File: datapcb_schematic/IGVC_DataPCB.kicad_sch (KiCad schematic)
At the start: 6 parts, among them J1 ODrive_S1_Left_Sensors_Output, J2 ODrive_S1_Right_Sensors_Output, J3 ODrive_S1_Right_J11_Input, J4 ODrive_S1_Left_J11_Input, J5 ODrive_S1_Left_J11_Output, J6 ODrive_S1_Left_J11_Output

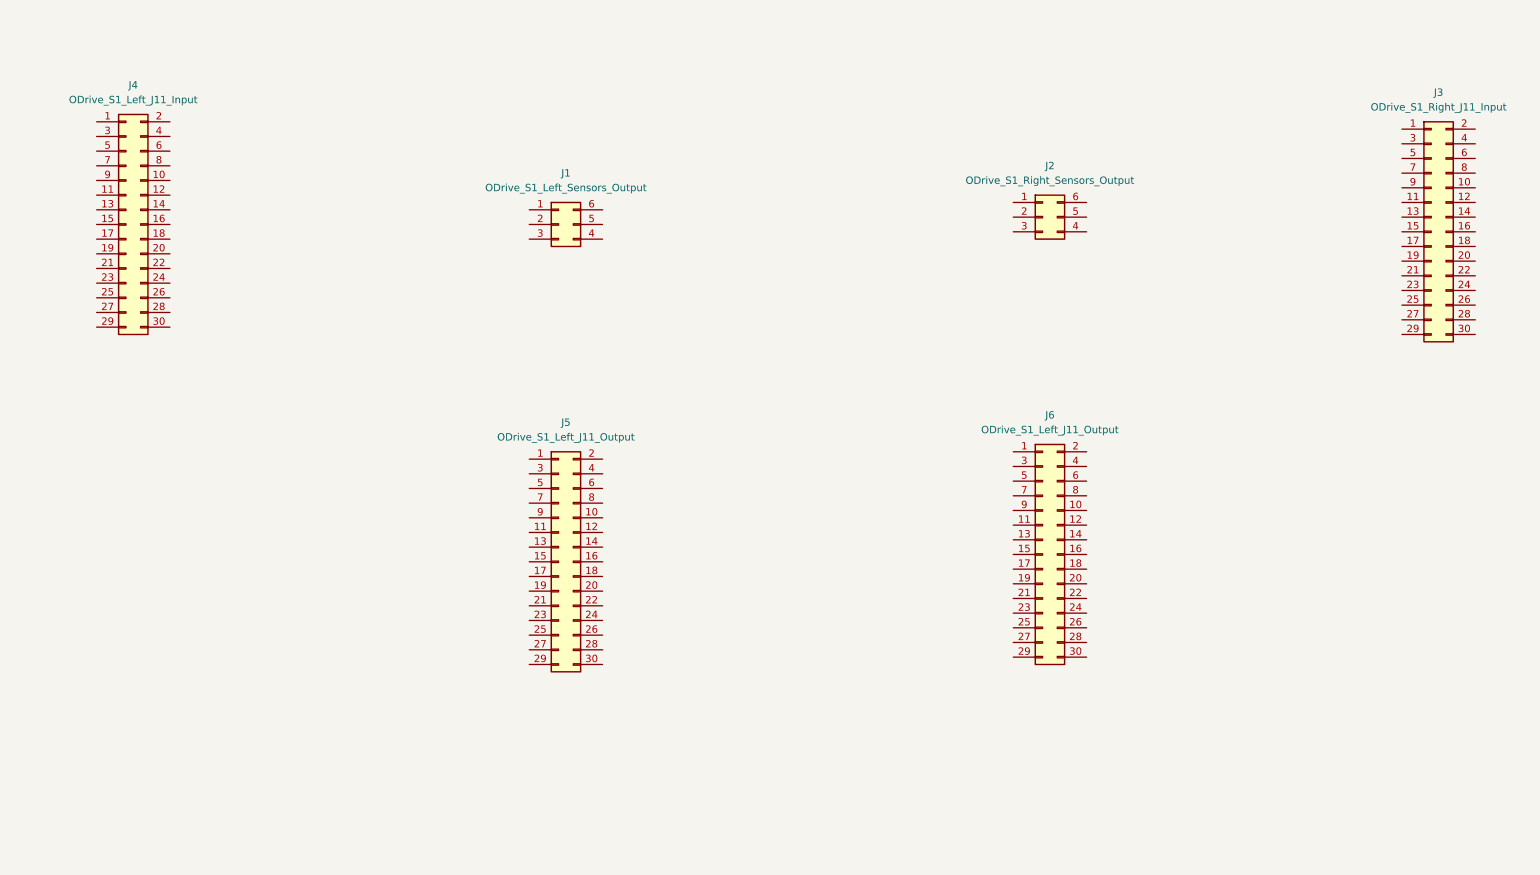
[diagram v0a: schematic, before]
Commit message: implemented net labels
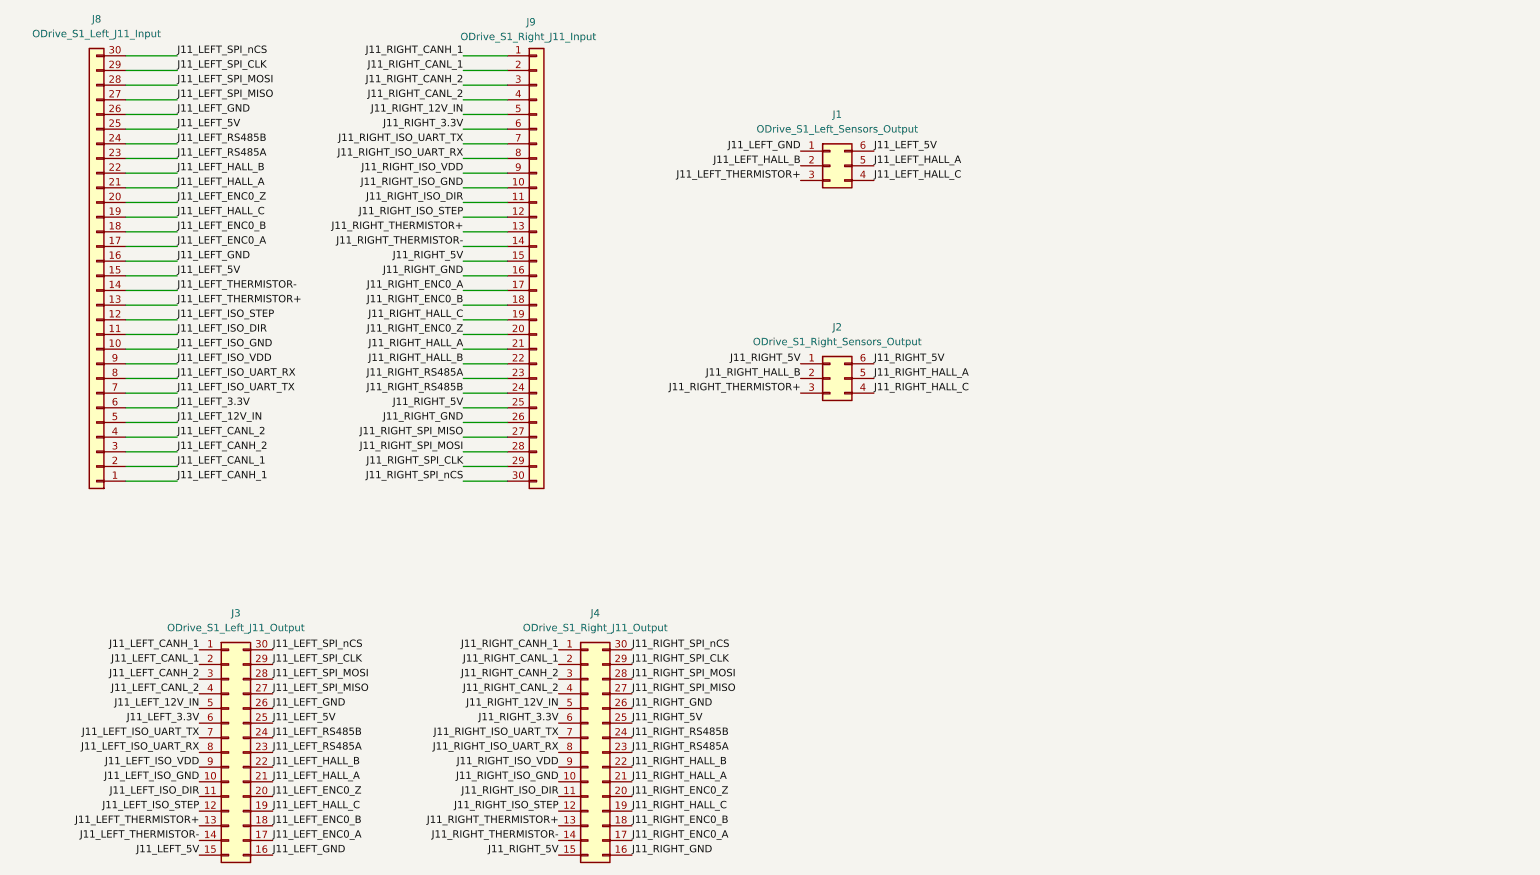
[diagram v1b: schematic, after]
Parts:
- removed J3: ODrive_S1_Right_J11_Input, symbol Connector_Generic:Conn_02x15_Odd_Even
- removed J4: ODrive_S1_Left_J11_Input, symbol Connector_Generic:Conn_02x15_Odd_Even
- removed J5, J6: ODrive_S1_Left_J11_Output, symbol Connector_Generic:Conn_02x15_Odd_Even
- added J3: ODrive_S1_Left_J11_Output, symbol Connector_Generic:Conn_02x15_Counter_Clockwise
- added J4: ODrive_S1_Right_J11_Output, symbol Connector_Generic:Conn_02x15_Counter_Clockwise
- added J8: ODrive_S1_Left_J11_Input, symbol Connector_Generic:Conn_01x30
- added J9: ODrive_S1_Right_J11_Input, symbol Connector_Generic:Conn_01x30
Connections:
- net J11_LEFT_GND: now reaches J1.1 (Pin_1)
- net J11_LEFT_GND: now also J3.16 (Pin_16), J3.26 (Pin_26), J8.16 (Pin_16), J8.26 (Pin_26)
- net J11_LEFT_HALL_B: now reaches J1.2 (Pin_2)
- net J11_LEFT_HALL_B: now also J3.22 (Pin_22), J8.22 (Pin_22)
- net J11_LEFT_THERMISTOR+: now reaches J1.3 (Pin_3)
- net J11_LEFT_THERMISTOR+: now also J3.13 (Pin_13), J8.13 (Pin_13)
- net J11_LEFT_HALL_C: now reaches J1.4 (Pin_4)
- net J11_LEFT_HALL_C: now also J3.19 (Pin_19), J8.19 (Pin_19)
- net J11_LEFT_HALL_A: now reaches J1.5 (Pin_5)
- net J11_LEFT_HALL_A: now also J3.21 (Pin_21), J8.21 (Pin_21)
- net J11_LEFT_5V: now reaches J1.6 (Pin_6)
- net J11_LEFT_5V: now also J3.15 (Pin_15), J3.25 (Pin_25), J8.15 (Pin_15), J8.25 (Pin_25)
- net J11_RIGHT_5V: now reaches J2.1 (Pin_1)
- net J11_RIGHT_5V: now also J2.6 (Pin_6), J4.15 (Pin_15), J4.25 (Pin_25), J9.15 (Pin_15), J9.25 (Pin_25)
- net J11_RIGHT_HALL_B: now reaches J2.2 (Pin_2)
- net J11_RIGHT_HALL_B: now also J4.22 (Pin_22), J9.22 (Pin_22)
- net J11_RIGHT_THERMISTOR+: now reaches J2.3 (Pin_3)
- net J11_RIGHT_THERMISTOR+: now also J4.13 (Pin_13), J9.13 (Pin_13)
- net J11_RIGHT_HALL_C: now reaches J2.4 (Pin_4)
- net J11_RIGHT_HALL_C: now also J4.19 (Pin_19), J9.19 (Pin_19)
- net J11_RIGHT_HALL_A: now reaches J2.5 (Pin_5)
- net J11_RIGHT_HALL_A: now also J4.21 (Pin_21), J9.21 (Pin_21)
- new net J11_LEFT_12V_IN: J3.5 (Pin_5), J8.5 (Pin_5)
- new net J11_LEFT_3.3V: J3.6 (Pin_6), J8.6 (Pin_6)
- new net J11_LEFT_CANH_1: J3.1 (Pin_1), J8.1 (Pin_1)
- new net J11_LEFT_CANH_2: J3.3 (Pin_3), J8.3 (Pin_3)
- new net J11_LEFT_CANL_1: J3.2 (Pin_2), J8.2 (Pin_2)
- new net J11_LEFT_CANL_2: J3.4 (Pin_4), J8.4 (Pin_4)
- new net J11_LEFT_ENC0_A: J3.17 (Pin_17), J8.17 (Pin_17)
- new net J11_LEFT_ENC0_B: J3.18 (Pin_18), J8.18 (Pin_18)
- new net J11_LEFT_ENC0_Z: J3.20 (Pin_20), J8.20 (Pin_20)
- new net J11_LEFT_ISO_DIR: J3.11 (Pin_11), J8.11 (Pin_11)
- new net J11_LEFT_ISO_GND: J3.10 (Pin_10), J8.10 (Pin_10)
- new net J11_LEFT_ISO_STEP: J3.12 (Pin_12), J8.12 (Pin_12)
- new net J11_LEFT_ISO_UART_RX: J3.8 (Pin_8), J8.8 (Pin_8)
- new net J11_LEFT_ISO_UART_TX: J3.7 (Pin_7), J8.7 (Pin_7)
- new net J11_LEFT_ISO_VDD: J3.9 (Pin_9), J8.9 (Pin_9)
- new net J11_LEFT_RS485A: J3.23 (Pin_23), J8.23 (Pin_23)
- new net J11_LEFT_RS485B: J3.24 (Pin_24), J8.24 (Pin_24)
- new net J11_LEFT_SPI_CLK: J3.29 (Pin_29), J8.29 (Pin_29)
- new net J11_LEFT_SPI_MISO: J3.27 (Pin_27), J8.27 (Pin_27)
- new net J11_LEFT_SPI_MOSI: J3.28 (Pin_28), J8.28 (Pin_28)
- new net J11_LEFT_SPI_nCS: J3.30 (Pin_30), J8.30 (Pin_30)
- new net J11_LEFT_THERMISTOR-: J3.14 (Pin_14), J8.14 (Pin_14)
- new net J11_RIGHT_12V_IN: J4.5 (Pin_5), J9.5 (Pin_5)
- new net J11_RIGHT_3.3V: J4.6 (Pin_6), J9.6 (Pin_6)
- new net J11_RIGHT_CANH_1: J4.1 (Pin_1), J9.1 (Pin_1)
- new net J11_RIGHT_CANH_2: J4.3 (Pin_3), J9.3 (Pin_3)
- new net J11_RIGHT_CANL_1: J4.2 (Pin_2), J9.2 (Pin_2)
- new net J11_RIGHT_CANL_2: J4.4 (Pin_4), J9.4 (Pin_4)
- new net J11_RIGHT_ENC0_A: J4.17 (Pin_17), J9.17 (Pin_17)
- new net J11_RIGHT_ENC0_B: J4.18 (Pin_18), J9.18 (Pin_18)
- new net J11_RIGHT_ENC0_Z: J4.20 (Pin_20), J9.20 (Pin_20)
- new net J11_RIGHT_GND: J4.16 (Pin_16), J4.26 (Pin_26), J9.16 (Pin_16), J9.26 (Pin_26)
- new net J11_RIGHT_ISO_DIR: J4.11 (Pin_11), J9.11 (Pin_11)
- new net J11_RIGHT_ISO_GND: J4.10 (Pin_10), J9.10 (Pin_10)
- new net J11_RIGHT_ISO_STEP: J4.12 (Pin_12), J9.12 (Pin_12)
- new net J11_RIGHT_ISO_UART_RX: J4.8 (Pin_8), J9.8 (Pin_8)
- new net J11_RIGHT_ISO_UART_TX: J4.7 (Pin_7), J9.7 (Pin_7)
- new net J11_RIGHT_ISO_VDD: J4.9 (Pin_9), J9.9 (Pin_9)
- new net J11_RIGHT_RS485A: J4.23 (Pin_23), J9.23 (Pin_23)
- new net J11_RIGHT_RS485B: J4.24 (Pin_24), J9.24 (Pin_24)
- new net J11_RIGHT_SPI_CLK: J4.29 (Pin_29), J9.29 (Pin_29)
- new net J11_RIGHT_SPI_MISO: J4.27 (Pin_27), J9.27 (Pin_27)
- new net J11_RIGHT_SPI_MOSI: J4.28 (Pin_28), J9.28 (Pin_28)
- new net J11_RIGHT_SPI_nCS: J4.30 (Pin_30), J9.30 (Pin_30)
- new net J11_RIGHT_THERMISTOR-: J4.14 (Pin_14), J9.14 (Pin_14)
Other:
- moved on the sheet: J1, J2
